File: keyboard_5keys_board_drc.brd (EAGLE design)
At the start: 95.2 x 14.5 mm, 23 parts, among them SW1 CHERRY-MX, SW2 CHERRY-MX, SW3 CHERRY-MX, SW4 CHERRY-MX, SW5 CHERRY-MX

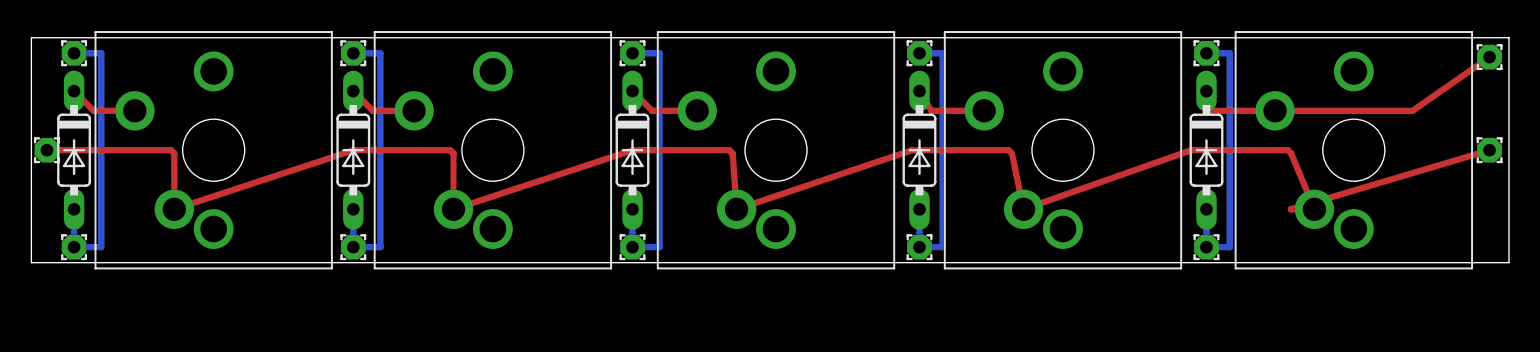
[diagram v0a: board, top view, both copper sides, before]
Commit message: Updated distances from dimensions
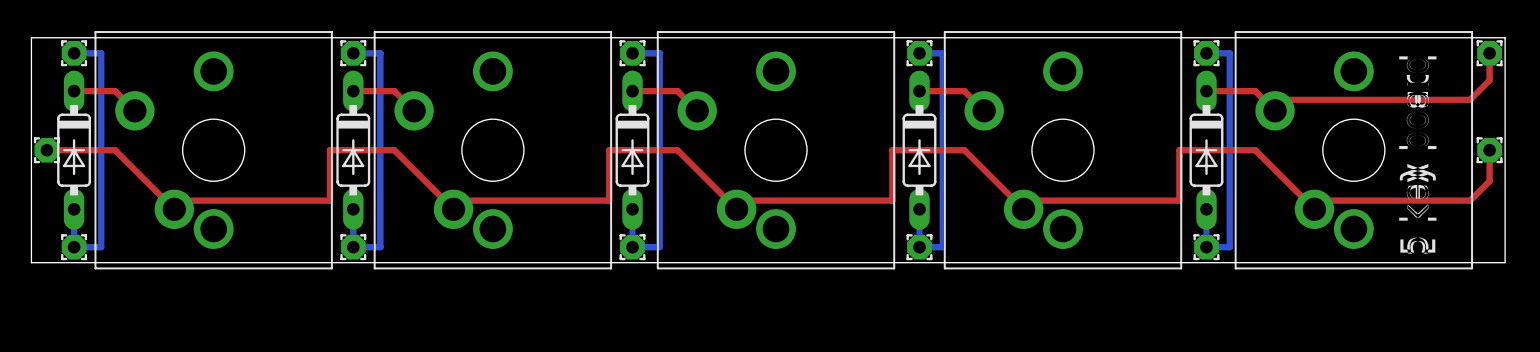
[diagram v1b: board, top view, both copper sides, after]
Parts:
- moved XTRA1 0.25 mm to (94.0, 14.0), turned to 90 degrees
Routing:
- net XOUT: track 115.4 -> 117.6 mm
- net N$5: track 20.4 -> 21.3 mm
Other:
- board size 95.2 x 14.5 mm -> 95 x 14.5 mm
- board text added: "5 key board"
- board text added: "九"
